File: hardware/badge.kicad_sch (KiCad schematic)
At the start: 2 parts

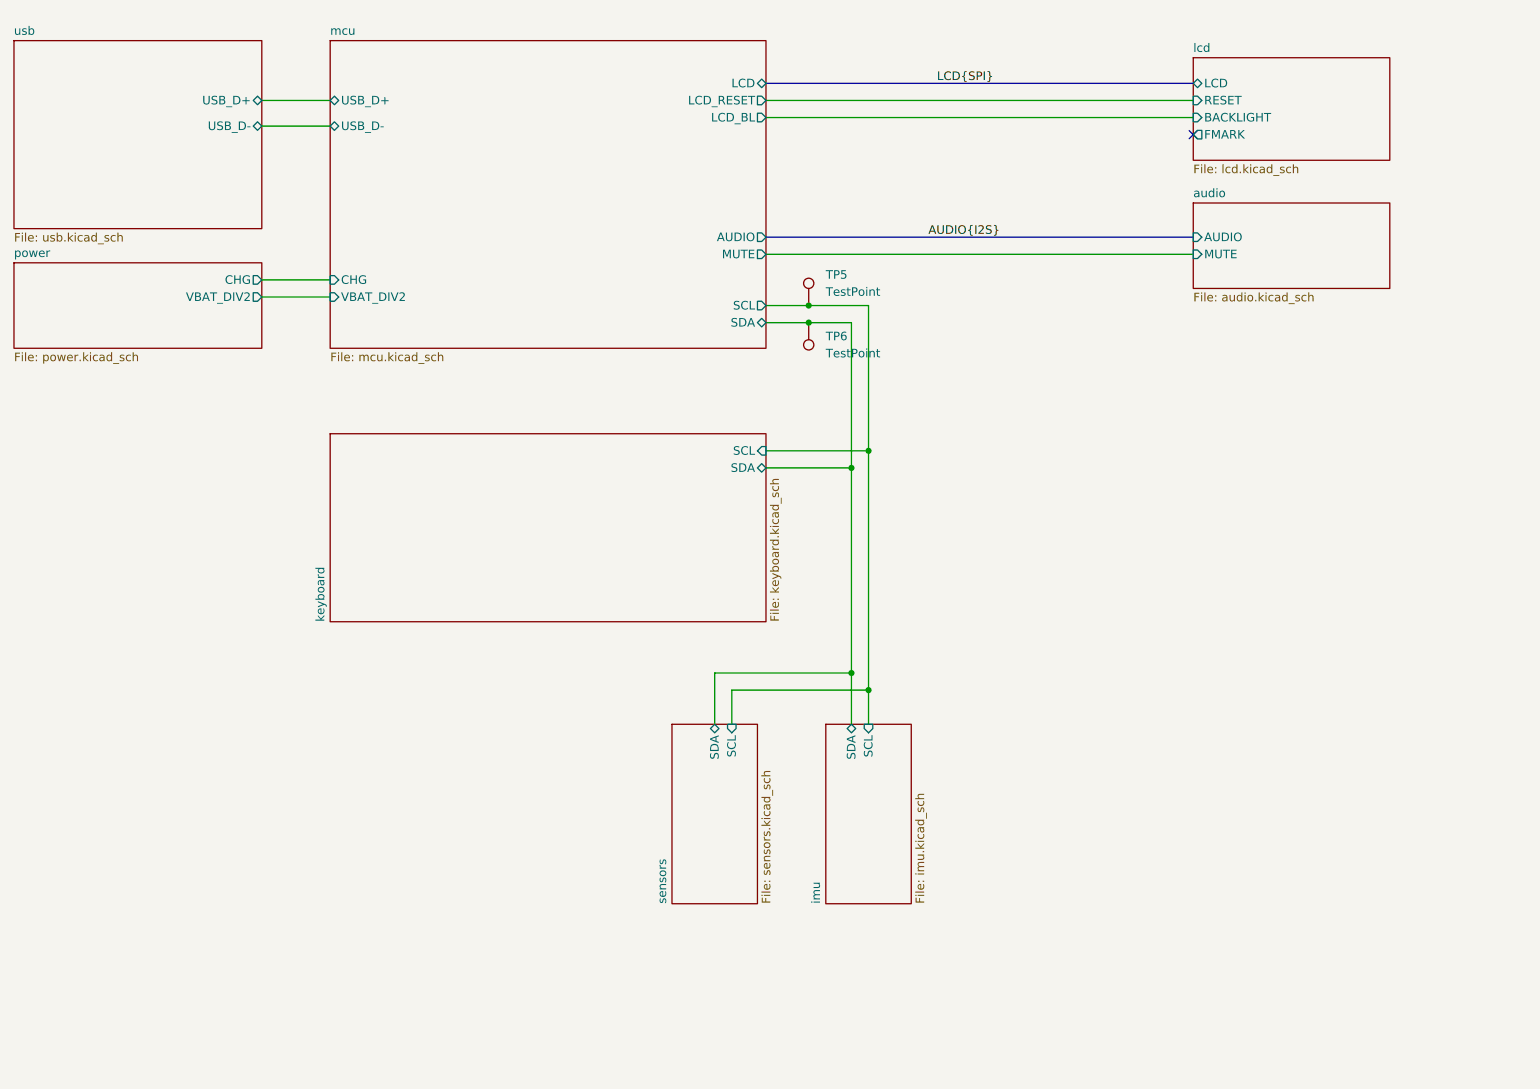
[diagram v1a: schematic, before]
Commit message: Add sdcard fooprint
Remove io expander
Reorganize a bit the mcu schematic
Routed audio
Routed lora
Partial pin swapping of esp32 for facilitating routing
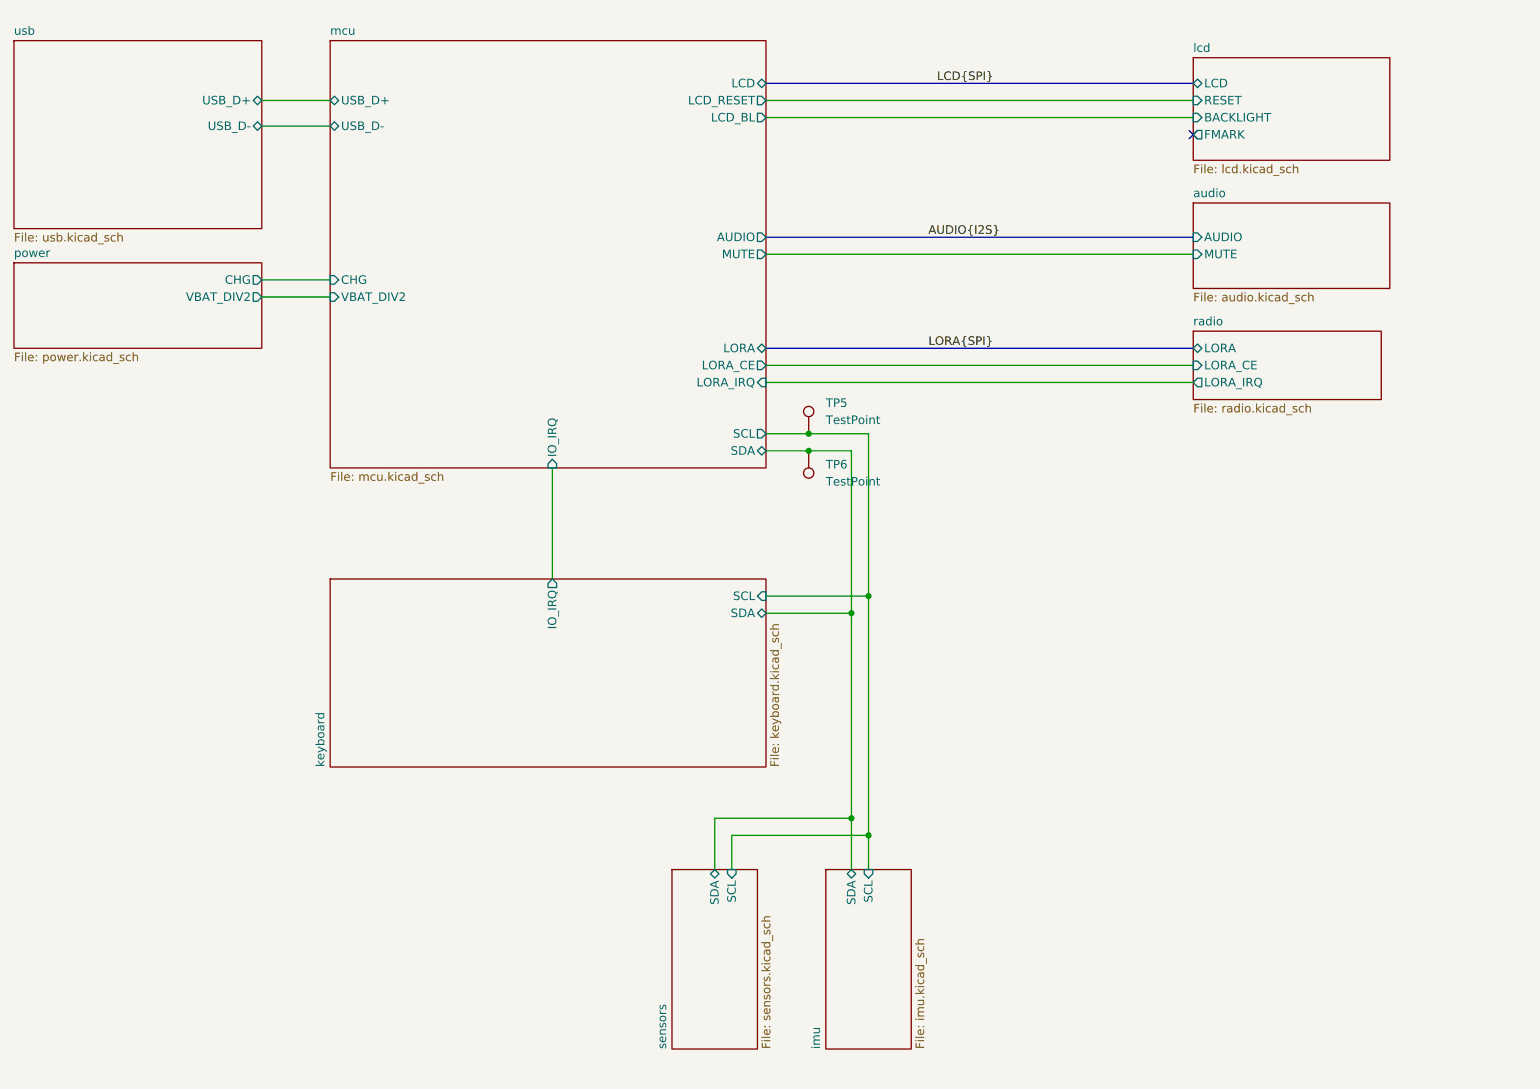
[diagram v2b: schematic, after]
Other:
- added sheet radio (radio.kicad_sch)
- sheet keyboard ports: added IO_IRQ; removed none
- sheet mcu ports: added IO_IRQ, LORA, LORA_CE, LORA_IRQ; removed none
- moved on the sheet: TP5, TP6

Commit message: Route all board
Fix CS missing for SD card
Add IMU symbol and footprint to the project lib
Finish esp32 pinswaps
Move non critical signals to the keyboard IO expander
Add power flag symbols
Fix Dpad pin type
Fix IMU pin type
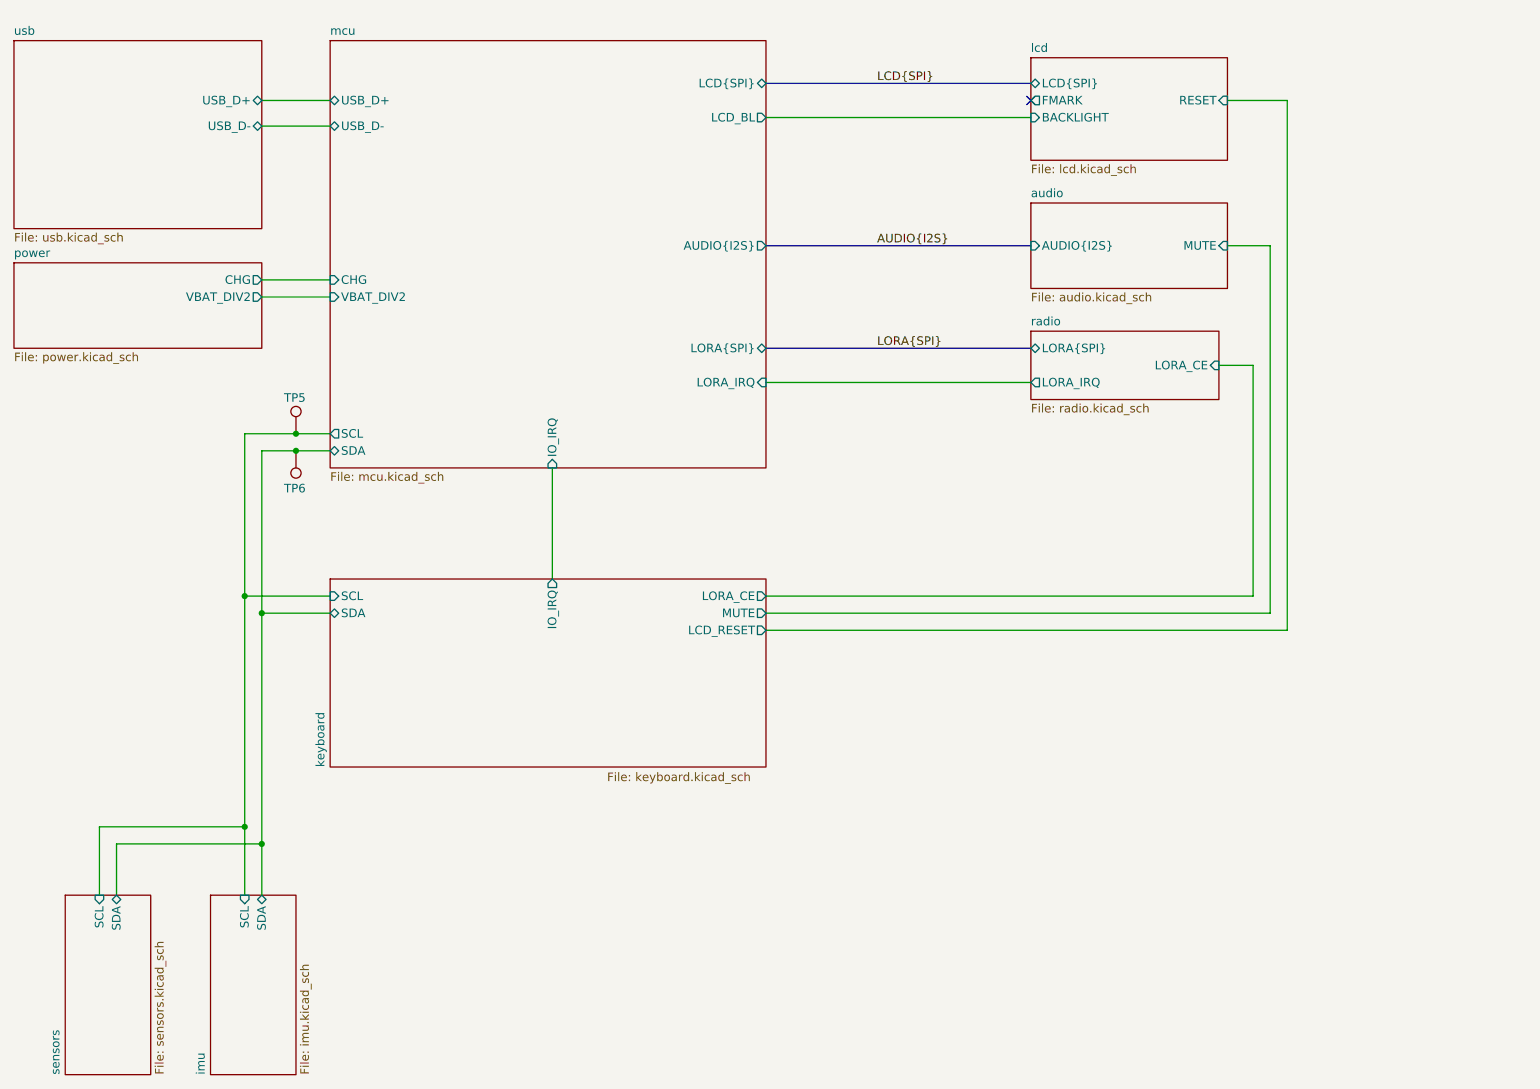
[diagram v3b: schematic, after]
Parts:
- TP5: value TestPoint -> SCL
- TP6: value TestPoint -> SDA
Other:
- sheet audio ports: added AUDIO{I2S}; removed AUDIO
- sheet keyboard ports: added LCD_RESET, LORA_CE, MUTE; removed none
- sheet lcd ports: added LCD{SPI}; removed LCD
- sheet mcu ports: added AUDIO{I2S}, LCD{SPI}, LORA{SPI}; removed AUDIO, LCD, LCD_RESET, LORA, LORA_CE, MUTE
- sheet radio ports: added LORA{SPI}; removed LORA
- moved on the sheet: TP5, TP6

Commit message: Associate all LCSC component
Change sdcard pullup resistor to 47K
Center main schematic
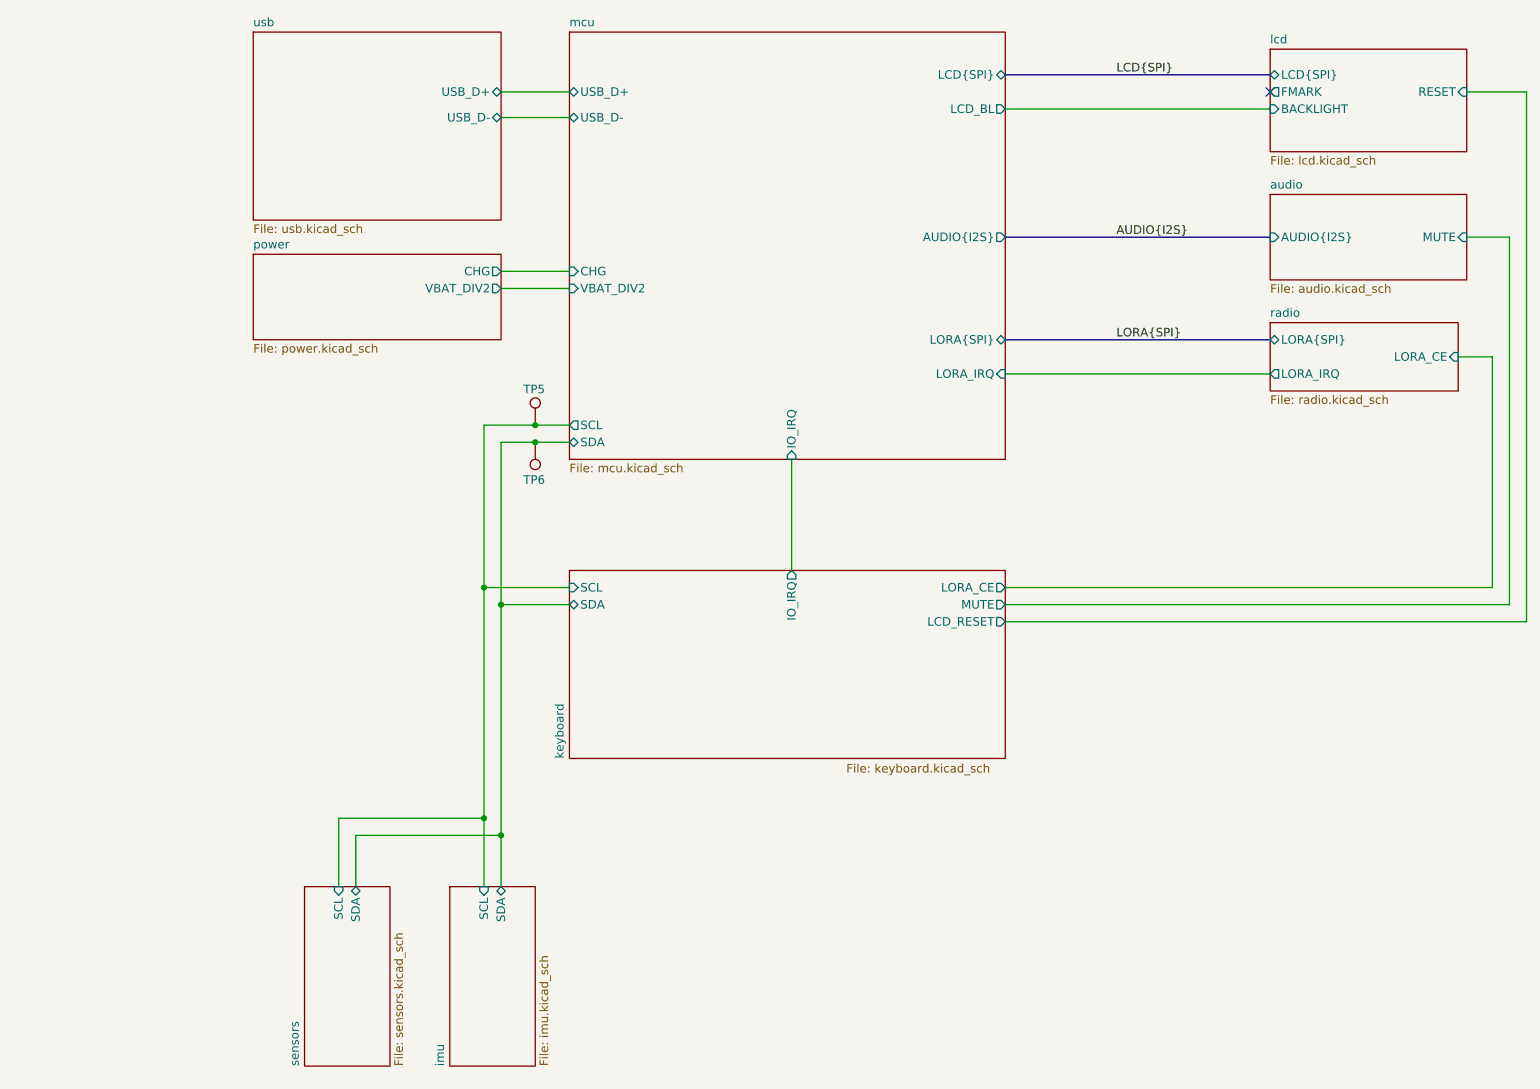
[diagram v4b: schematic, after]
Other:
- moved on the sheet: TP5, TP6
